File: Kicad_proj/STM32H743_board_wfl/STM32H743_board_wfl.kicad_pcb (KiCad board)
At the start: 4 copper layers, 38.5 x 38.5 mm, 64 parts, among them J1 GPS, J2 ESC, J3 UART, J4 Tag_Connect_6pin, U1 LT8609SEV#PBF, U2 AP7361C-33E, U3 STM32H743VITx, U4 W25Q512JVEIQ, U5 BMI088, Y1 TSX-3225_16.0000MF18X-AC0

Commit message: LT8609 footprint cuts
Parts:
- moved U1 167.6 mm to (2.17, 1.75)
- moved U2 41.6 mm to (147.3, 130.4), turned to -90 degrees
- moved C5 38.6 mm to (174.4, 92.1)
- moved C7 38.6 mm to (178.3, 105.0)
- moved C9 38.6 mm to (171.3, 95.0)
- moved R1 38.6 mm to (174.4, 95.4)
- moved R2 38.6 mm to (174.4, 97.0)
- moved R4 38.6 mm to (174.4, 100.3)
- moved C6 38.6 mm to (171.3, 92.5)
- moved C8 38.6 mm to (174.4, 93.7)
- moved L1 38.6 mm to (179.7, 98.3)
- moved R3 38.6 mm to (174.4, 98.7)
- moved C11 36.3 mm to (145.5, 124.6), turned to 0 degrees
- moved C10 33.5 mm to (148.8, 124.6), turned to 180 degrees
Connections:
- C22 pad 1: Net-(U3-PA0) -> unconnected-(C22-Pad1)
- C22 pad 2: GND -> unconnected-(C22-Pad2)

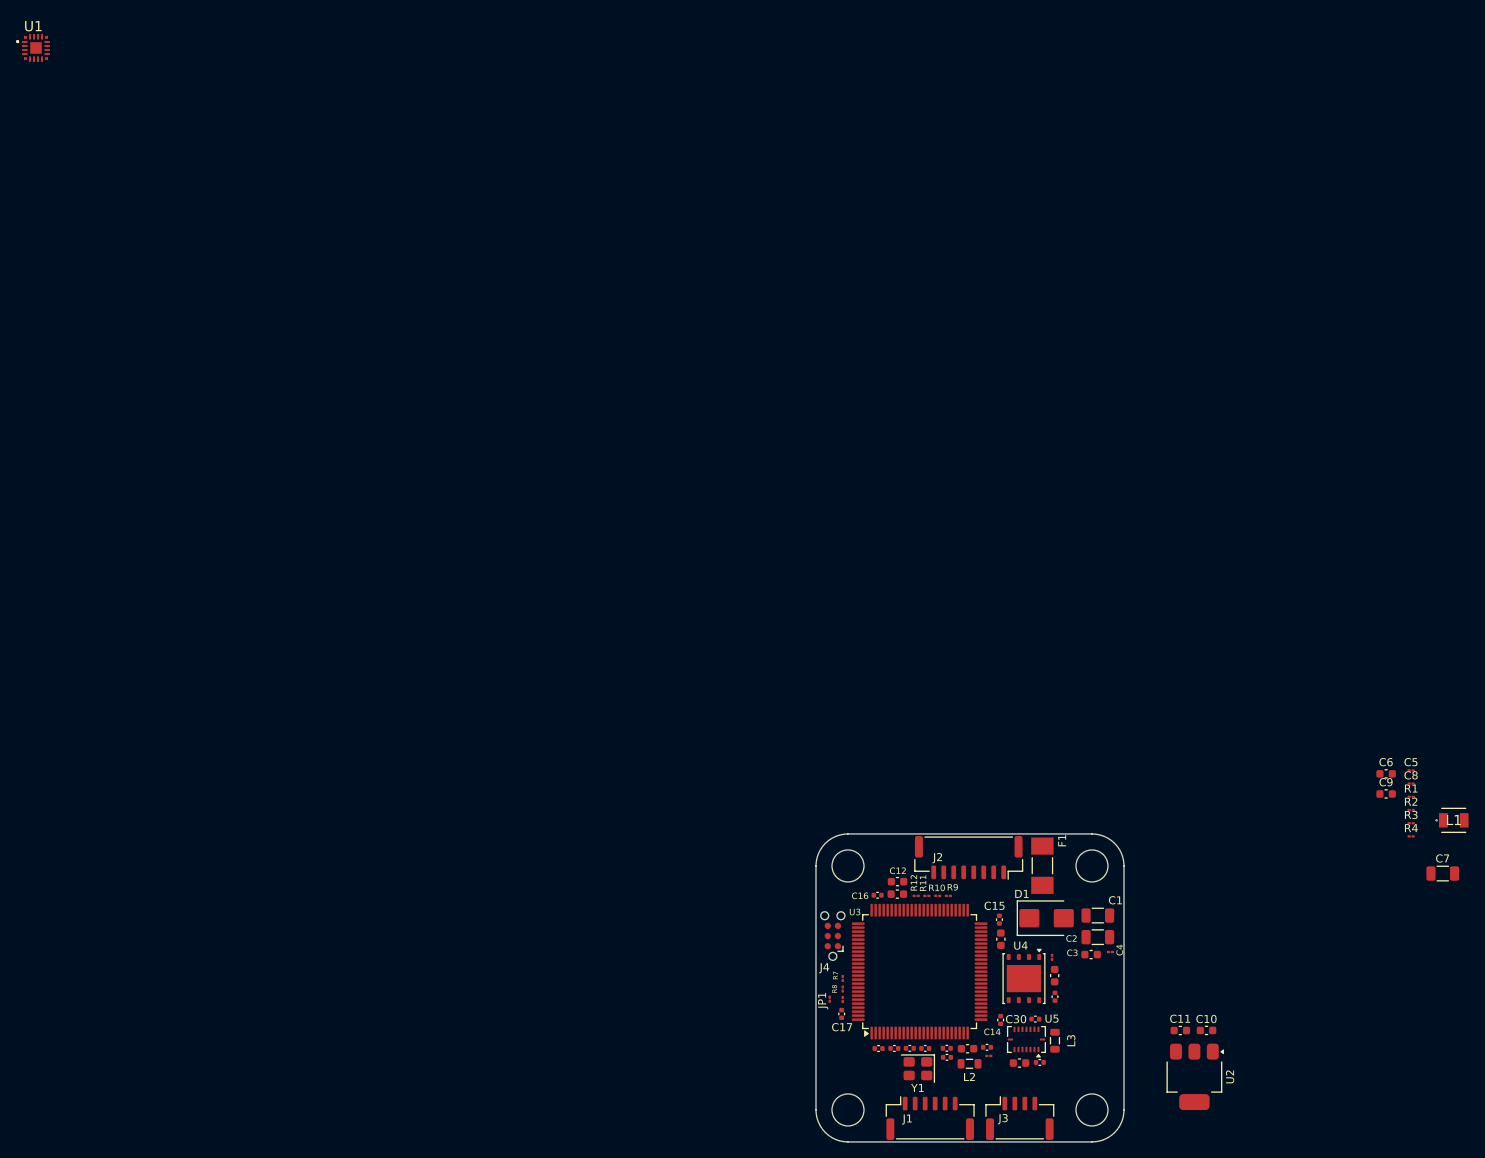
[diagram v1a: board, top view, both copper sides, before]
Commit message: PCB v0.4 components placement first phase done
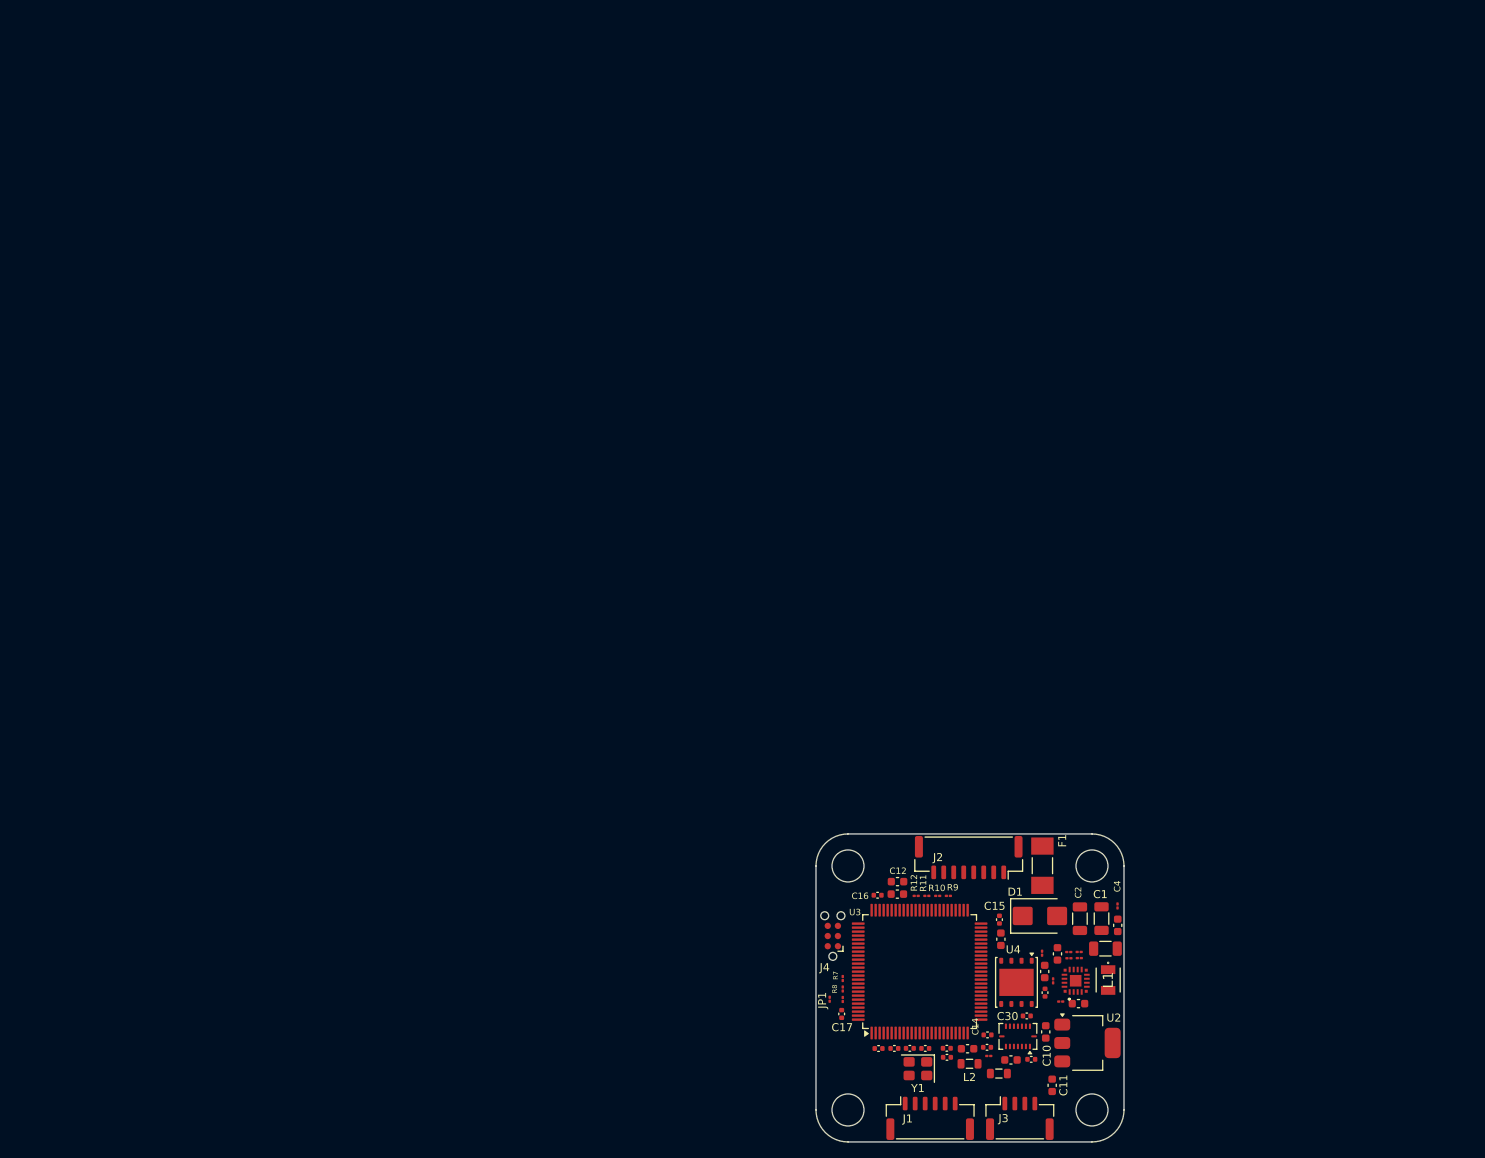
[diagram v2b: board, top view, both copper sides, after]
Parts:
- moved U1 175.1 mm to (132.5, 118.7), turned to 90 degrees
- moved C8 51.1 mm to (129.6, 118.4), turned to 90 degrees
- moved R2 49.9 mm to (130.6, 121.0), turned to 180 degrees
- moved C6 48.0 mm to (132.8, 121.2)
- moved L1 47.6 mm to (136.5, 118.3), turned to -90 degrees
- moved C5 47.3 mm to (132.9, 114.8)
- moved R1 47.0 mm to (131.6, 114.8), turned to 180 degrees
- moved C9 45.7 mm to (130.2, 115.0), turned to 90 degrees
- moved R4 45.4 mm to (131.6, 115.5), turned to 180 degrees
- moved R3 44.8 mm to (132.9, 115.5)
- moved C7 43.2 mm to (136.2, 114.3)
- moved C10 20.1 mm to (128.7, 124.7), turned to -90 degrees
- moved C11 17.4 mm to (129.5, 131.4), turned to -90 degrees
- moved U2 14.0 mm to (133.9, 126.1), turned to 0 degrees
- moved L3 8.12 mm to (122.9, 129.9), turned to 0 degrees
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
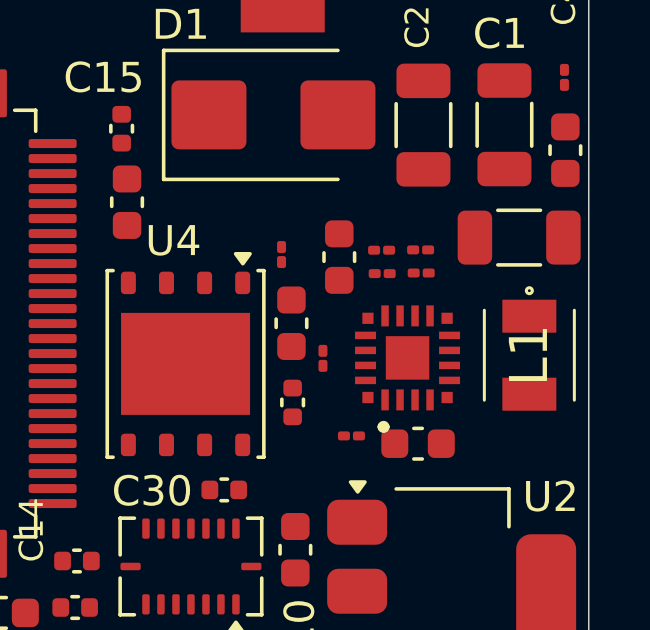
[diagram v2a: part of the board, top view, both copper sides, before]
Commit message: set route and vias sizes
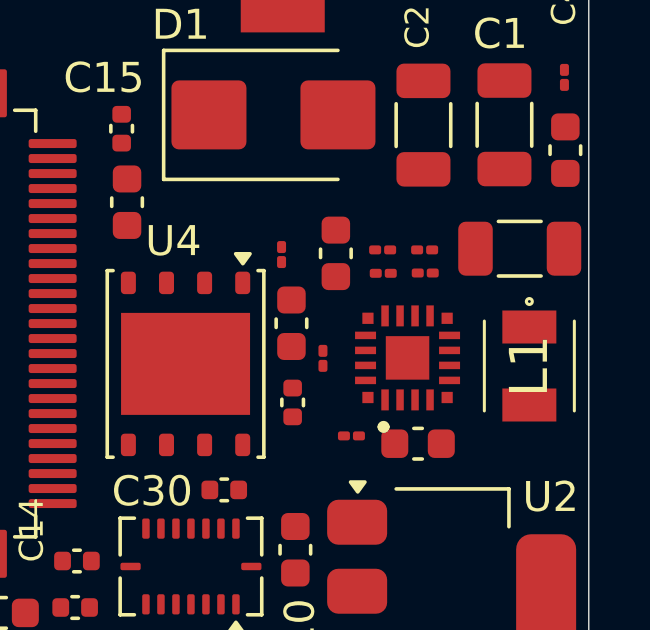
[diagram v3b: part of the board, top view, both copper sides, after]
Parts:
- moved C7 0.37 mm to (136.2, 114.7)
- moved L1 0.36 mm to (136.5, 118.6)
- moved C9 0.17 mm to (130.1, 114.9)
- moved R3 0.14 mm to (133.1, 115.5)
- moved C5 0.13 mm to (133.0, 114.8)
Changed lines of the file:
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@@
 	(footprint "Resistor_SMD:R_01005_0402Metric"
 		(layer "F.Cu")
-		(at 131.595 114.76 180)
+		(at 131.63 114.75 180)
 		(descr "Resistor SMD 01005 (0402 Metric), square (rectangular) end terminal, IPC-7351 nominal, (Body size source: http://www.vishay.com/docs/20056/crcw01005e3.pdf)")
 		(tags "resistor")
@@
 	(footprint "Capacitor_SMD:C_01005_0402Metric"
 		(layer "F.Cu")
-		(at 132.895 114.75)
+		(at 133.03 114.75)
 		(descr "Capacitor SMD 01005 (0402 Metric), square (rectangular) end terminal, IPC-7351 nominal, (Body size source: http://www.vishay.com/docs/20056/crcw01005e3.pdf)")
 		(tags "capacitor")
@@
 	(footprint "Capacitor_SMD:C_1206_3216Metric"
 		(layer "F.Cu")
-		(at 136.18 114.34)
+		(at 136.2 114.71)
 		(descr "Capacitor SMD 1206 (3216 Metric), square (rectangular) end terminal, IPC-7351 nominal, (Body size source: IPC-SM-782 page 76, https://www.pcb-3d.com/wordpress/wp-content/uploads/ipc-sm-782a_amendment_1_and_2.pdf)")
 		(tags "capacitor")
@@
 			)
 		)
+		(property "ref rab" "U1"
+			(at 0 0 0)
+			(unlocked yes)
+			(layer "F.Fab")
+			(effects
+				(font
+					(size 1 1)
+					(thickness 0.15)
+				)
+			)
+		)
 		(sheetname "/02_Power_regulation/")
 		(sheetfile "02_power_regulation.kicad_sch")
@@
 	(footprint "STM32H743_board_library_footprints:SPM3010-3020"
 		(layer "F.Cu")
-		(at 136.52 118.26 -90)
+		(at 136.52 118.62 -90)
 		(descr "SPM3010-3020")
 		(tags "Inductor (FeSi Core)")
@@
 	(footprint "Resistor_SMD:R_01005_0402Metric"
 		(layer "F.Cu")
-		(at 132.915 115.52)
+		(at 133.05 115.52)
 		(descr "Resistor SMD 01005 (0402 Metric), square (rectangular) end terminal, IPC-7351 nominal, (Body size source: http://www.vishay.com/docs/20056/crcw01005e3.pdf)")
 		(tags "resistor")
@@
 	(footprint "Resistor_SMD:R_01005_0402Metric"
 		(layer "F.Cu")
-		(at 131.615 115.54 180)
+		(at 131.65 115.53 180)
 		(descr "Resistor SMD 01005 (0402 Metric), square (rectangular) end terminal, IPC-7351 nominal, (Body size source: http://www.vishay.com/docs/20056/crcw01005e3.pdf)")
 		(tags "resistor")
@@
 	(footprint "Capacitor_SMD:C_0603_1608Metric"
 		(layer "F.Cu")
-		(at 130.185 114.99 90)
+		(at 130.07 114.865 90)
 		(descr "Capacitor SMD 0603 (1608 Metric), square (rectangular) end terminal, IPC-7351 nominal, (Body size source: IPC-SM-782 page 76, https://www.pcb-3d.com/wordpress/wp-content/uploads/ipc-sm-782a_amendment_1_and_2.pdf)")
 		(tags "capacitor")

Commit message: PCB v0.5 SMPS hot loop optimization + fab texts removal
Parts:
- moved R4 1.66 mm to (133.3, 115.8), turned to 0 degrees
- moved C9 1.22 mm to (131.1, 115.5), turned to 180 degrees
- moved R3 0.92 mm to (132.9, 114.6), turned to 90 degrees
- moved C5 0.60 mm to (133.6, 114.6), turned to 90 degrees
- moved C8 0.58 mm to (130.2, 118.4)
- moved U1 0.37 mm to (132.8, 118.7)
- moved R1 0.35 mm to (131.8, 114.5)
- moved R2 0.18 mm to (130.6, 120.8)
- moved L1 0.18 mm to (136.7, 118.6)
- moved C7 0.05 mm to (136.2, 114.7)

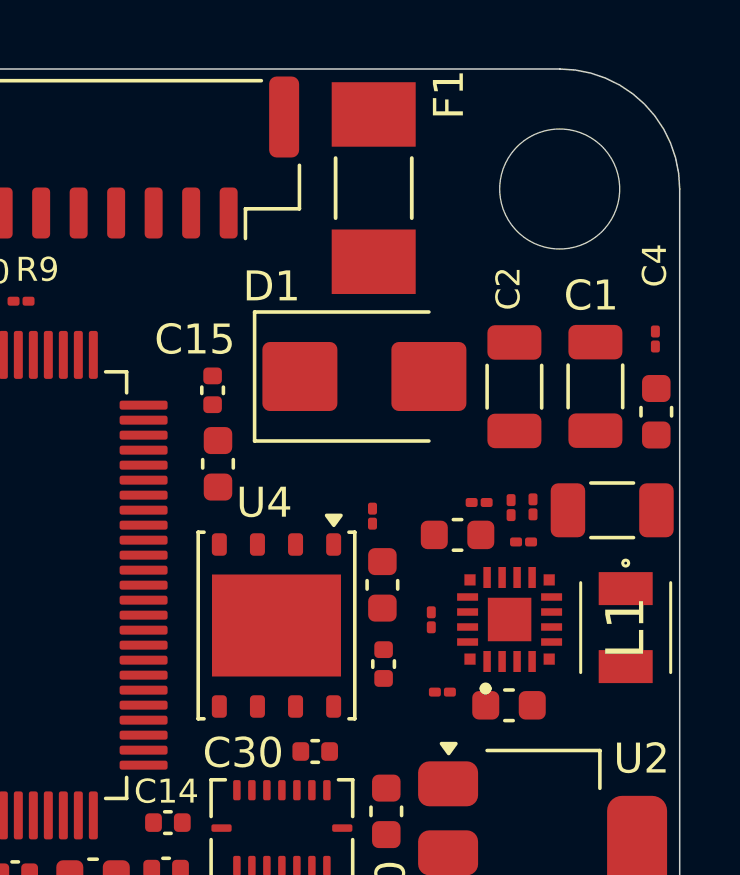
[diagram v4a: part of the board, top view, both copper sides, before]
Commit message: PCB v0.6 routing part1
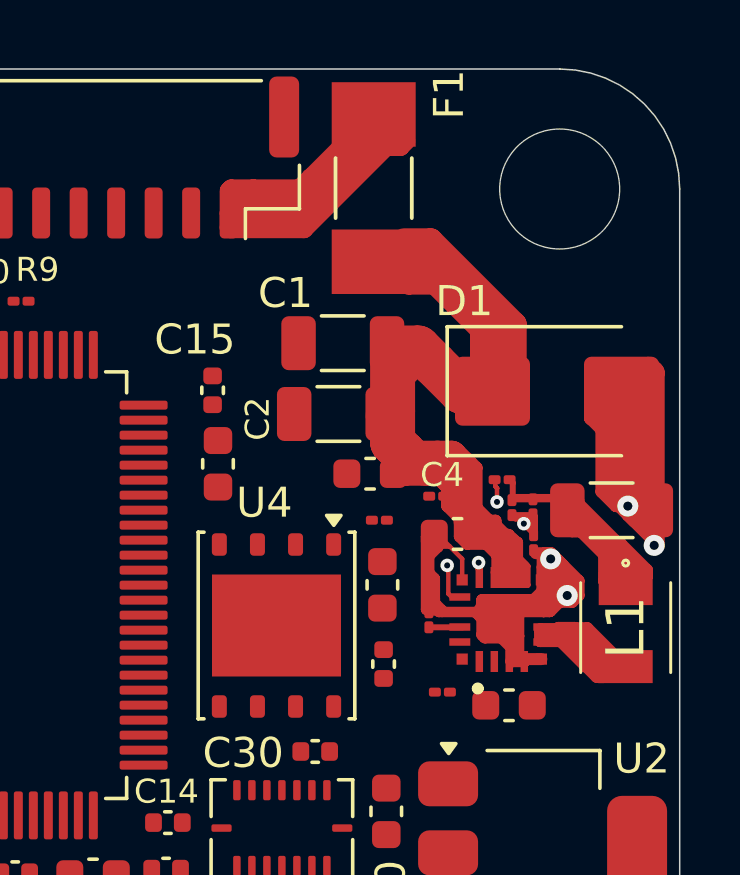
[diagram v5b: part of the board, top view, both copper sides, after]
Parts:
- moved C3 9.76 mm to (128.2, 113.5), turned to 180 degrees
- moved C4 8.98 mm to (130.4, 114.2), turned to 180 degrees
- moved C1 8.54 mm to (127.3, 109.1), turned to 180 degrees
- moved D1 6.44 mm to (134.4, 110.7)
- moved C2 5.94 mm to (127.1, 111.5), turned to 180 degrees
- moved R1 1.08 mm to (132.6, 113.7)
- moved R4 0.34 mm to (133.6, 115.8), turned to -90 degrees
- moved R13 0.27 mm to (128.5, 115.0), turned to 180 degrees
- moved U1 0.26 mm to (132.6, 118.7)
- moved C8 0.08 mm to (130.1, 118.4)
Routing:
- net GND: track 0.00 -> 62.5 mm, vias 0 -> 4
- net +26V_prefiltered: track 0.00 -> 53.9 mm
- net +BATT: track 0.00 -> 25.8 mm
- net +5V: track 0.00 -> 22.1 mm
- net Net-(U1-SW_1): track 0.00 -> 15.0 mm
- net Net-(U1-FB): track 0.00 -> 5.44 mm, vias 0 -> 2
- net Net-(U1-PG): track 0.00 -> 1.29 mm, vias 0 -> 2
- net Net-(U1-TR/SS): track 0.00 -> 1.14 mm

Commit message: PCB v0.7 routing part2
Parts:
- moved R13 2.62 mm to (125.9, 114.7), turned to 0 degrees
- turned C25 to 180 degrees
- turned J4 to -90 degrees
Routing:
- net GND: track 62.5 -> 154.2 mm, vias 4 -> 7
- net +3V3: track 0.00 -> 14.5 mm
- net /03_STM32H743_schematic/SWDIO: track 0.00 -> 7.33 mm
- net /03_STM32H743_schematic/SWCLK: track 0.00 -> 5.18 mm
- net Net-(C25-Pad1): track 0.00 -> 4.07 mm

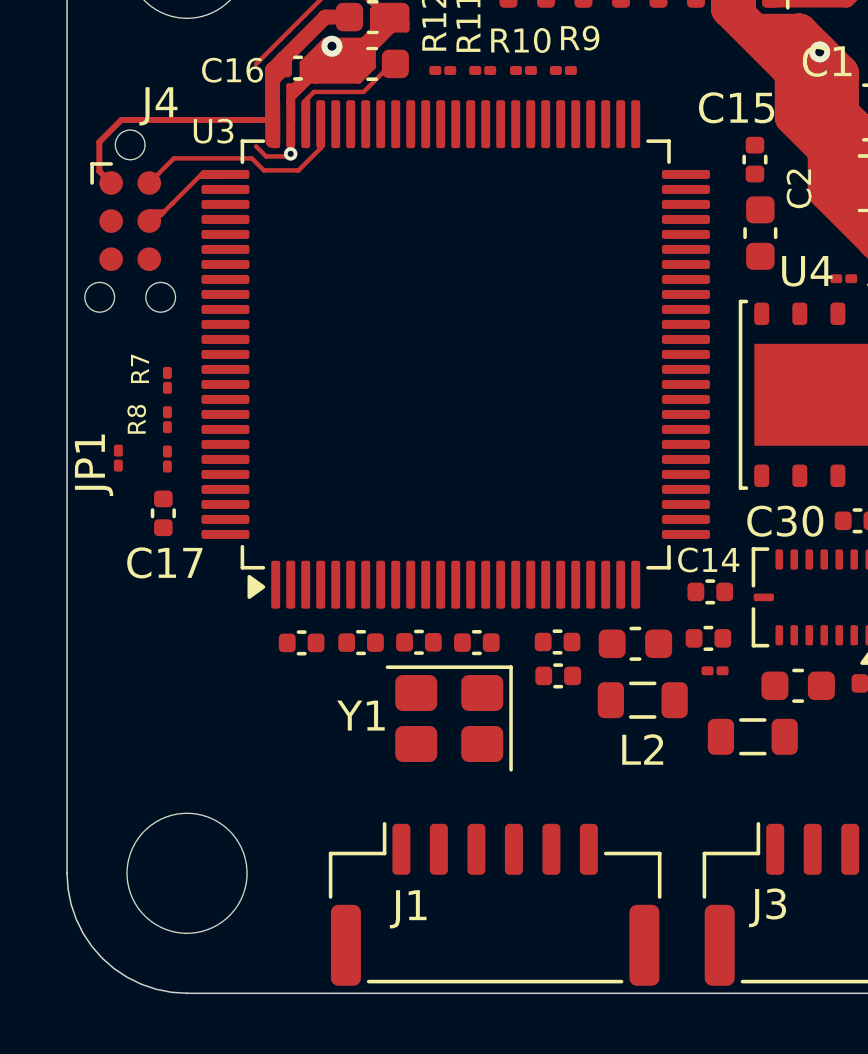
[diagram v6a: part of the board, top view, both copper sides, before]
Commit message: PCB v0.7 routing part3
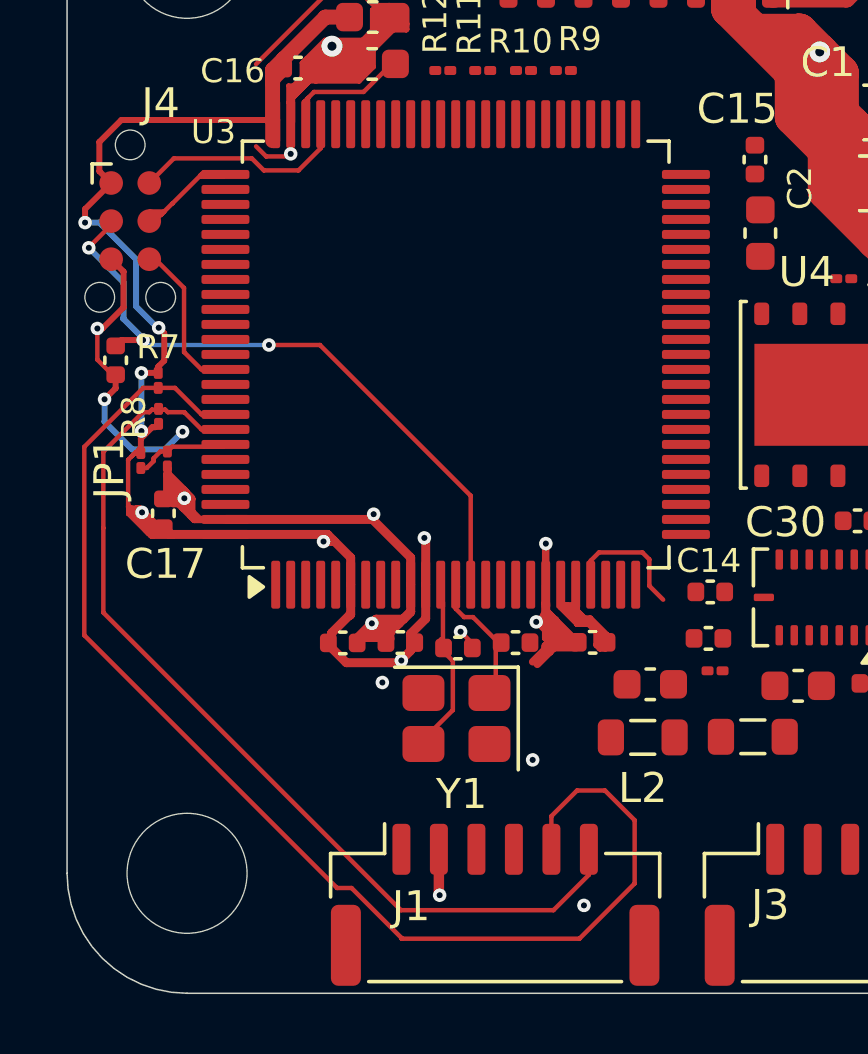
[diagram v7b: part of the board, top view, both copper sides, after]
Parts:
- moved C21 18.1 mm to (101.6, 117.4), turned to -90 degrees
- moved C19 1.44 mm to (119.4, 128.2)
- moved C20 1.37 mm to (109.2, 126.8), turned to 0 degrees
- moved C23 1.31 mm to (113.0, 127.0), turned to 0 degrees
- moved C13 1.31 mm to (111.1, 126.8)
- moved C24 1.29 mm to (115.0, 126.8)
- moved L2 1.24 mm to (119.2, 130.0)
- moved C18 1.17 mm to (117.5, 126.8)
- moved JP1 0.75 mm to (102.5, 120.7)
- moved R8 0.31 mm to (103.0, 119.3)
- moved R7 0.30 mm to (103.0, 118.1)
- moved Y1 0.24 mm to (113.0, 129.3)
- turned R6 to -90 degrees
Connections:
- C22 pad 1: unconnected-(C22-Pad1) -> Net-(U3-PA0)
- C22 pad 2: unconnected-(C22-Pad2) -> GND
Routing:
- net GND: track 154.2 -> 207.6 mm, vias 7 -> 20
- net +3V3: track 14.5 -> 57.7 mm, vias 0 -> 8
- net /03_STM32H743_schematic/I2C1_SCL: track 0.00 -> 42.2 mm
- net /03_STM32H743_schematic/I2C1_SDA: track 0.00 -> 31.9 mm
- net /03_STM32H743_schematic/SWD_NRST: track 0.00 -> 22.1 mm, vias 0 -> 3
- net Net-(U3-VDDA): track 0.00 -> 8.17 mm
- net /03_STM32H743_schematic/SWO: track 0.00 -> 5.31 mm
- net Net-(U3-PH0): track 0.00 -> 4.96 mm
- net Net-(U3-PH1): track 0.00 -> 4.73 mm
- net Net-(U3-PA0): track 0.00 -> 4.50 mm
- net Net-(JP1-A): track 0.00 -> 3.20 mm
